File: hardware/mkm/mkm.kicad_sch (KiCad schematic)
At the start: 26 parts, among them J1 DIN-5_180degree, J2 DIN-5_180degree, J3 DIN-5_180degree, U1 40106, U2 H11L1

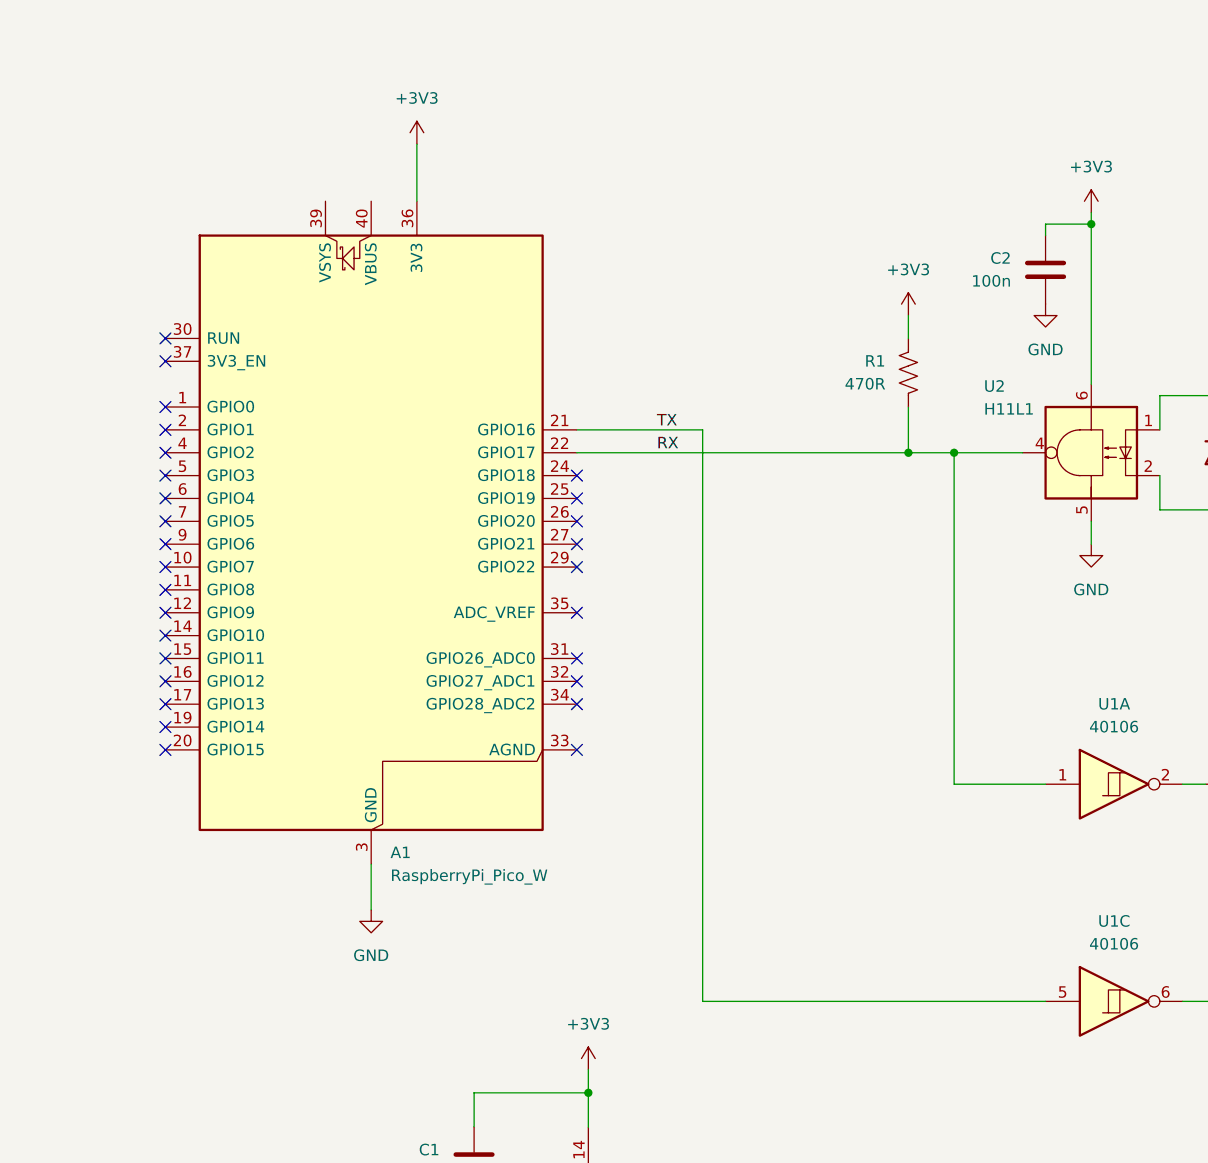
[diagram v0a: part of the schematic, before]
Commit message: Sending simulated MIDI packets via BLE to the app (all in debug mode)
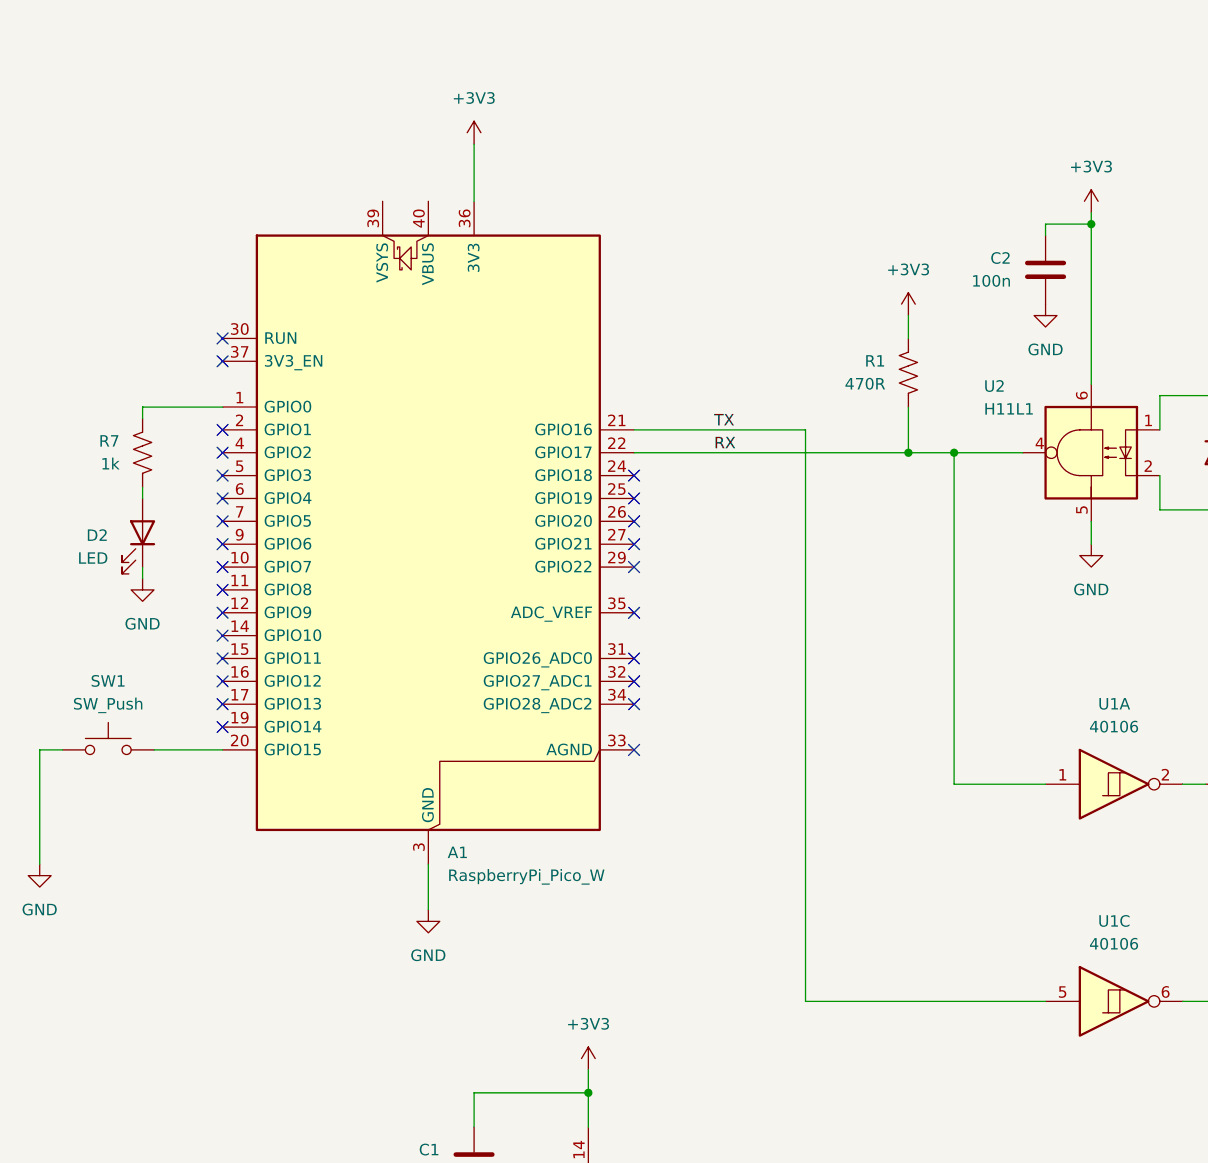
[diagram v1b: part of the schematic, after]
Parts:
- added D2: LED, LED_THT:LED_D5.0mm_Clear, symbol Device:LED
- added R7: 1k, Resistor_THT:R_Axial_DIN0207_L6.3mm_D2.5mm_P7.62mm_Horizontal, symbol Device:R_US
- added SW1: SW_Push, Button_Switch_THT:SW_PUSH_6mm, symbol Switch:SW_Push
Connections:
- net GND: now also D2.1 (K), SW1.1
- net at A1.1 (GPIO0): now also R7.2
- net at A1.20 (GPIO15): now also SW1.2
- new net: D2.2 (A), R7.1
- no-connect marks 34 -> 32
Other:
- moved on the sheet: A1
